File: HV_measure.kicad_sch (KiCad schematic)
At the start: 42 parts

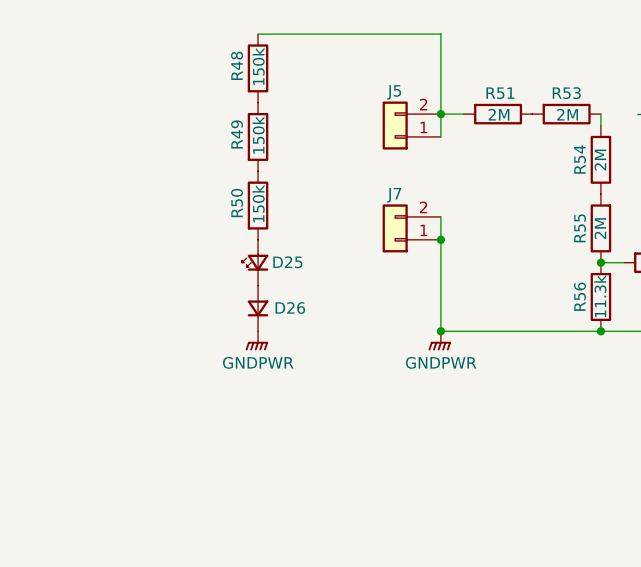
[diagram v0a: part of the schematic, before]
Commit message: VER1.0: добавил аппаратную защиту
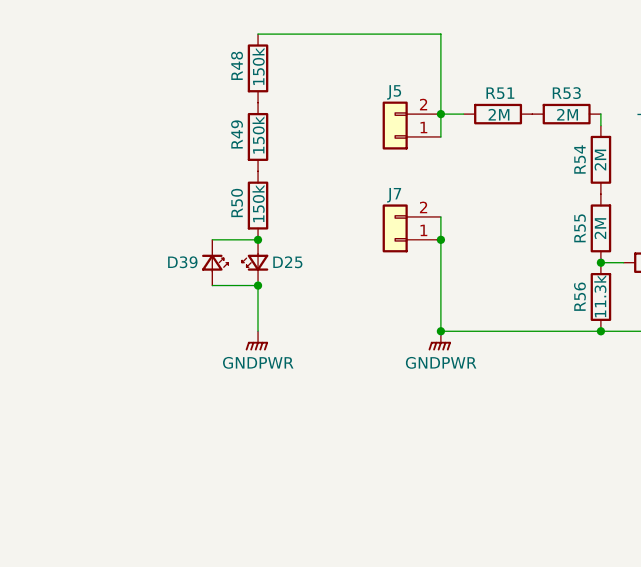
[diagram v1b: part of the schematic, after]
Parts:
- removed D26: (no value), Diode_SMD:D_SMA_Handsoldering, symbol Device:D_Small
- added D39: (no value), LED_SMD:LED_1206_3216Metric_Pad1.42x1.75mm_HandSolder, symbol Device:LED_Small
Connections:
- net GNDPWR: now also D25.1 (K), D39.2 (A)
- net at D25.2 (A), R50.2: now also D39.1 (K)
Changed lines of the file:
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@@
 	)
 	(junction
+		(at 68.58 116.84)
+		(diameter 0)
+		(color 0 0 0 0)
+	)
+	(junction
 		(at 143.51 133.35)
 		(diameter 0)
@@
 	)
 	(junction
+		(at 68.58 111.76)
+		(diameter 0)
+		(color 0 0 0 0)
+	)
+	(junction
 		(at 171.45 99.695)
 		(diameter 0)
@@
 	(wire
 		(pts
+			(xy 63.5 116.84) (xy 68.58 116.84)
+		)
+		(stroke
+			(width 0)
+			(type default)
+		)
+	)
+	(wire
+		(pts
 			(xy 165.1 120.65) (xy 177.8 120.65)
 		)
@@
 	(wire
 		(pts
+			(xy 63.5 111.76) (xy 68.58 111.76)
+		)
+		(stroke
+			(width 0)
+			(type default)
+		)
+	)
+	(wire
+		(pts
 			(xy 152.4 115.57) (xy 152.4 116.84)
 		)
@@
 	(wire
 		(pts
+			(xy 68.58 116.84) (xy 68.58 121.92)
+		)
+		(stroke
+			(width 0)
+			(type default)
+		)
+	)
+	(wire
+		(pts
 			(xy 125.73 46.99) (xy 125.73 48.26)
 		)
@@
 	)
 	(symbol
-		(lib_id "Device:D_Small")
-		(at 68.58 119.38 90)
-		(unit 1)
-		(body_style 1)
-		(exclude_from_sim no)
-		(in_bom yes)
-		(on_board yes)
-		(in_pos_files yes)
-		(dnp no)
-		(property "Reference" "D26"
-			(at 70.358 119.38 90)
-			(show_name no)
-			(do_not_autoplace no)
-			(effects
-				(font
-					(size 1.27 1.27)
-				)
-				(justify right)
-			)
-		)
-		(property "Value" ""
-			(at 71.12 120.65 90)
-			(hide yes)
-			(show_name no)
-			(do_not_autoplace no)
-			(effects
-				(font
-					(size 1.27 1.27)
-				)
-				(justify right)
-			)
-		)
-		(property "Footprint" "Diode_SMD:D_SMA_Handsoldering"
-			(at 68.58 119.38 90)
-			(hide yes)
-			(show_name no)
-			(do_not_autoplace no)
-			(effects
-				(font
-					(size 1.27 1.27)
-				)
-			)
-		)
-		(property "Datasheet" ""
-			(at 68.58 119.38 90)
-			(hide yes)
-			(show_name no)
-			(do_not_autoplace no)
-			(effects
-				(font
-					(size 1.27 1.27)
-				)
-			)
-		)
-		(property "Description" "Diode, small symbol"
-			(at 68.58 119.38 0)
-			(hide yes)
-			(show_name no)
-			(do_not_autoplace no)
-			(effects
-				(font
-					(size 1.27 1.27)
-				)
-			)
-		)
-		(property "Sim.Device" "D"
-			(at 68.58 119.38 0)
-			(hide yes)
-			(show_name no)
-			(do_not_autoplace no)
-			(effects
-				(font
-					(size 1.27 1.27)
-				)
-			)
-		)
-		(property "Sim.Pins" "1=K 2=A"
-			(at 68.58 119.38 0)
-			(hide yes)
-			(show_name no)
-			(do_not_autoplace no)
-			(effects
-				(font
-					(size 1.27 1.27)
-				)
-			)
-		)
-		(property "Description P/N" "Diode"
-			(at 68.58 119.38 90)
-			(hide yes)
-			(show_name no)
-			(do_not_autoplace no)
-			(effects
-				(font
-					(size 1.27 1.27)
-				)
-			)
-		)
-		(property "Product Name" "S1M"
-			(at 68.58 119.38 90)
-			(hide yes)
-			(show_name no)
-			(do_not_autoplace no)
-			(effects
-				(font
-					(size 1.27 1.27)
-				)
-			)
-		)
-		(pin "2"
-		)
-		(pin "1"
-		)
-		(instances
-			(project "PSFB_MCU"
-				(path "/1f44d793-713f-4781-bd7e-20142de81965/70b7ff82-f266-429f-9b56-1fc4058a165c"
-					(reference "D26")
-					(unit 1)
-				)
-			)
-		)
-	)
-	(symbol
 		(lib_id "power:GND")
 		(at 185.42 128.27 0)
@@
 					(unit 1)
 				)
+			)
+		)
+	)
+	(symbol
+		(lib_id "Device:LED_Small")
+		(at 63.5 114.3 270)
+		(unit 1)
+		(body_style 1)
+		(exclude_from_sim no)
+		(in_bom yes)
+		(on_board yes)
+		(in_pos_files yes)
+		(dnp no)
+		(property "Reference" "D39"
+			(at 61.976 114.3 90)
+			(show_name no)
+			(do_not_autoplace no)
+			(effects
+				(font
+					(size 1.27 1.27)
+				)
+				(justify right)
+			)
+		)
+		(property "Value" ""
+			(at 60.96 113.0935 90)
+			(hide yes)
+			(show_name no)
+			(do_not_autoplace no)
+			(effects
+				(font
+					(size 1.27 1.27)
+				)
+				(justify right)
+			)
+		)
+		(property "Footprint" "LED_SMD:LED_1206_3216Metric_Pad1.42x1.75mm_HandSolder"
+			(at 63.5 114.3 90)
+			(hide yes)
+			(show_name no)
+			(do_not_autoplace no)
+			(effects
+				(font
+					(size 1.27 1.27)
+				)
+			)
+		)
+		(property "Datasheet" ""
+			(at 63.5 114.3 90)
+			(hide yes)
+			(show_name no)
+			(do_not_autoplace no)
+			(effects
+				(font
+					(size 1.27 1.27)
+				)
+			)
+		)
+		(property "Description" "Red LED"
+			(at 63.5 114.3 0)
+			(hide yes)
+			(show_name no)
+			(do_not_autoplace no)
+			(effects
+				(font
+					(size 1.27 1.27)
+				)
+			)
+		)
+		(property "Sim.Pin" "1=K 2=A"
+			(at 63.5 114.3 0)
+			(hide yes)
+			(show_name no)
+			(do_not_autoplace no)
+			(effects
+				(font
+					(size 1.27 1.27)
+				)
+			)
+		)
+		(property "Description P/N" "Red LED"
+			(at 63.5 114.3 90)
+			(hide yes)
+			(show_name no)
+			(do_not_autoplace no)
+			(effects
+				(font
+					(size 1.27 1.27)
+				)
+			)
+		)
+		(property "Product Name" "TO-3216BC-MRE"
+			(at 63.5 114.3 90)
+			(hide yes)
+			(show_name no)
+			(do_not_autoplace no)
+			(effects
+				(font
+					(size 1.27 1.27)
+				)
+			)
+		)
+		(pin "2"
+		)
+		(pin "1"
+		)
+		(instances
+			(project "PSFB_MCU"
+				(path "/1f44d793-713f-4781-bd7e-20142de81965/70b7ff82-f266-429f-9b56-1fc4058a165c"
+					(reference "D39")
+					(unit 1)
+				)

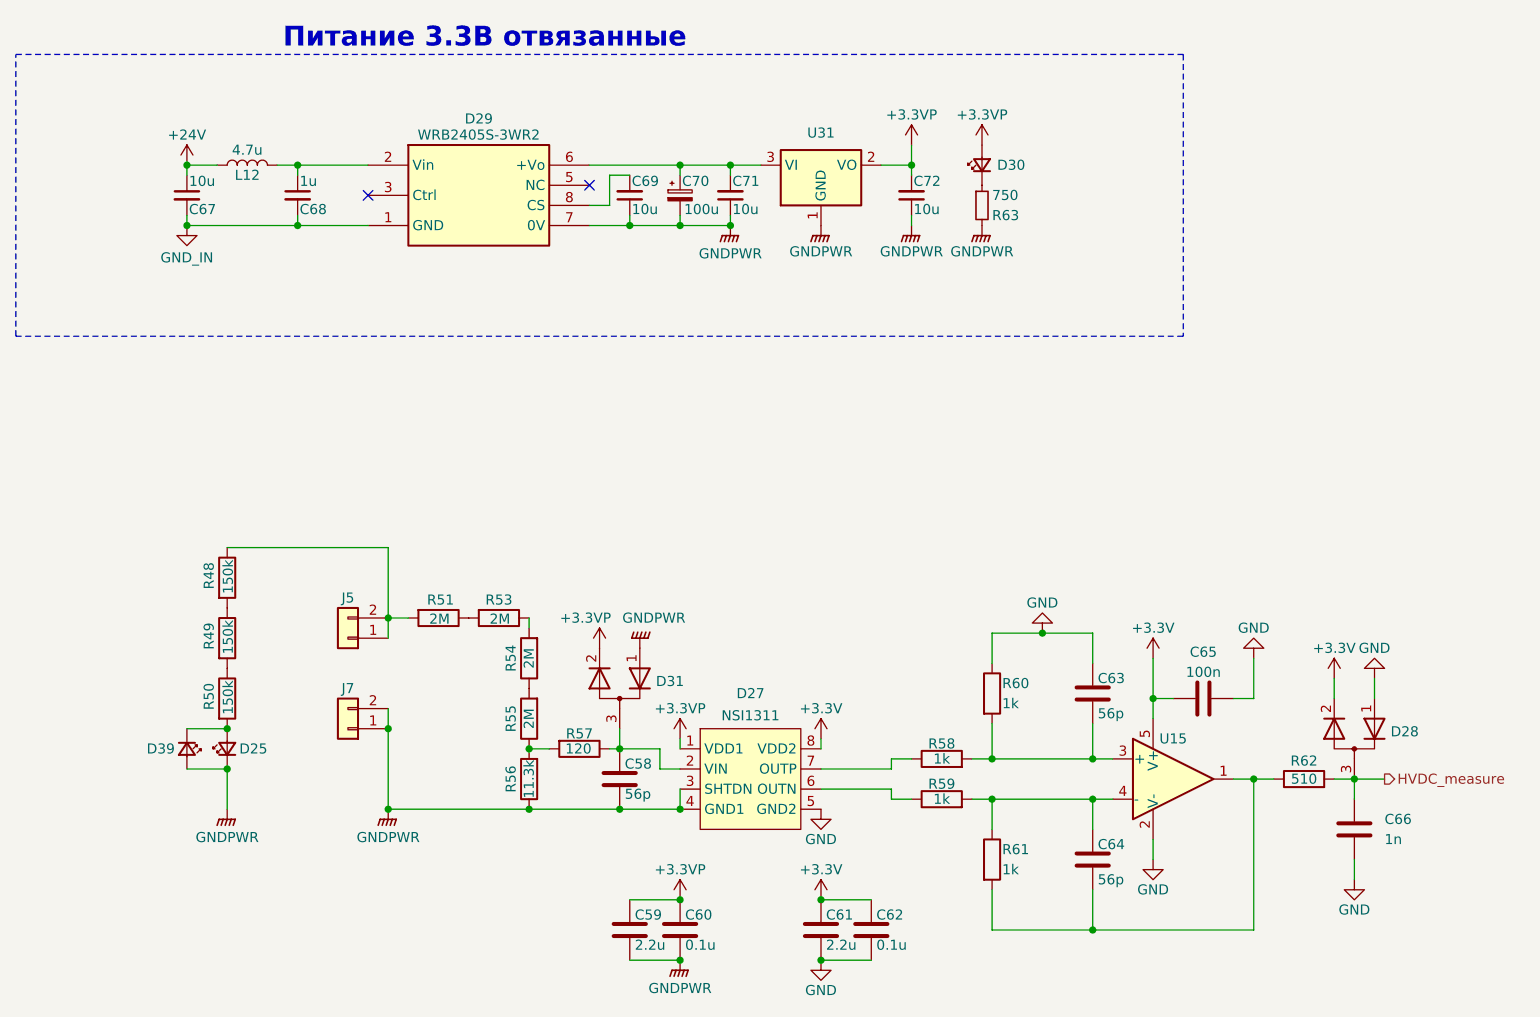
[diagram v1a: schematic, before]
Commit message: VER1.0: добавил разделение питания VDD и VDDA
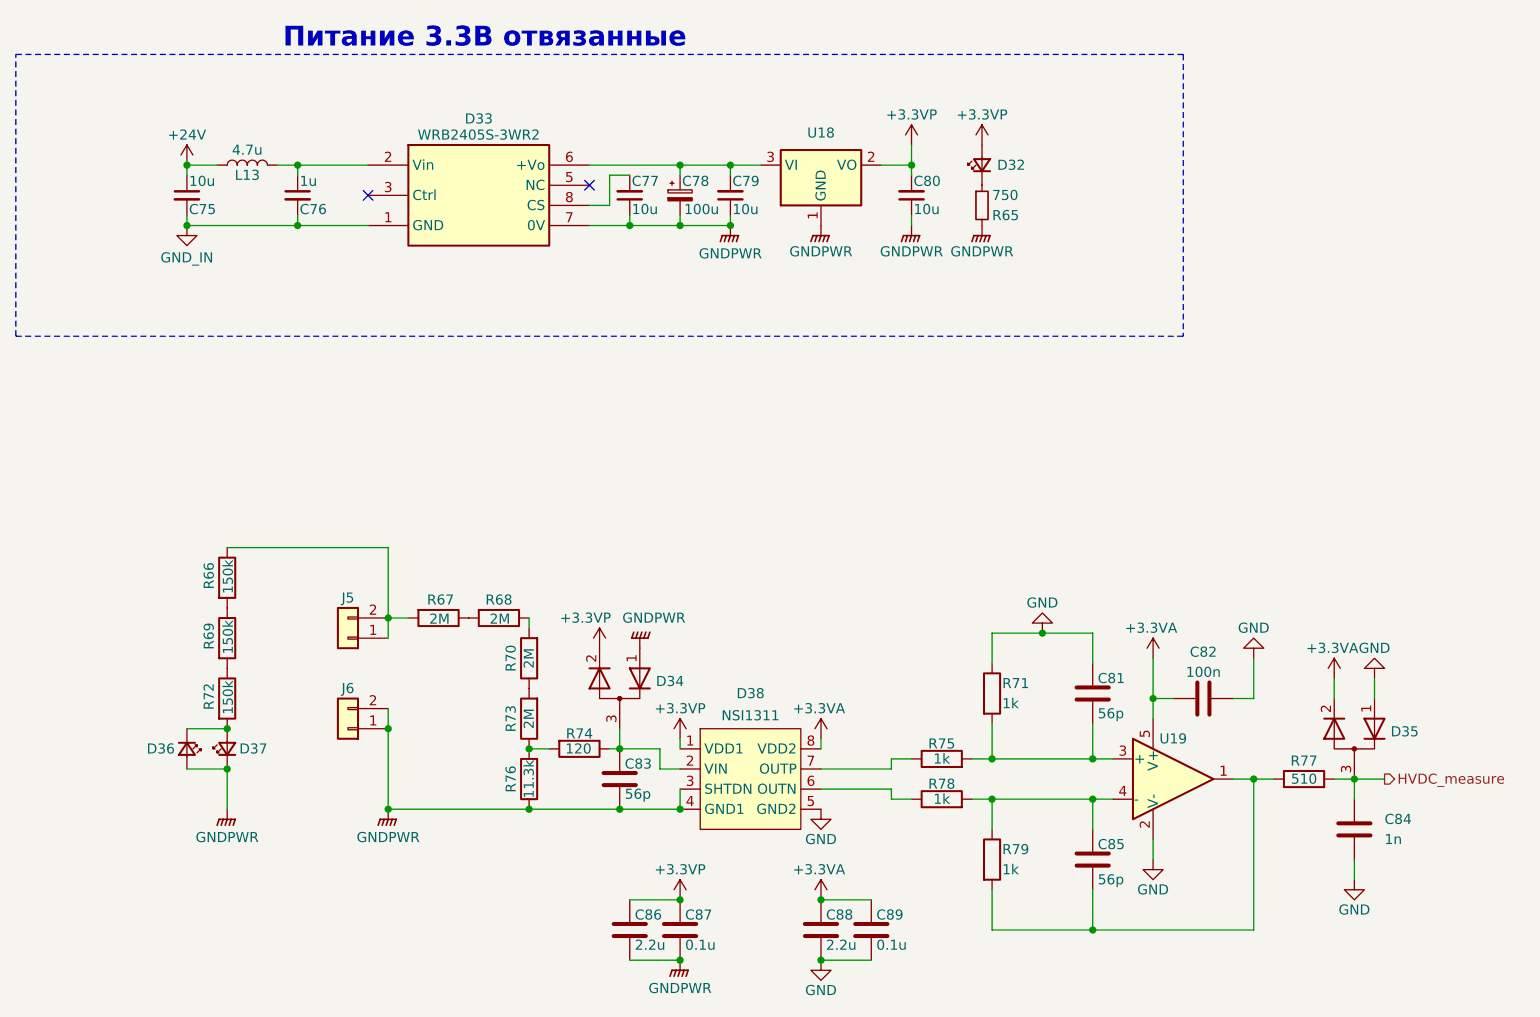
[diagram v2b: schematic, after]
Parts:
- C75: renamed from C67; Description P/N Capacitor SMD 50V -> Capacitor SMD 25V
- C77: renamed from C69; Description P/N Capacitor SMD 50V -> Capacitor SMD 25V
- C78: renamed from C70; Description P/N Polarized capacitor -> Capacitor tantalum SMD 6.3V; Product Name 293D107X96R3B2TE3 -> 6TPE100MWB
- C79: renamed from C71; Description P/N Capacitor SMD 50V -> Capacitor SMD 25V
- C80: renamed from C72; Description P/N Capacitor SMD 50V -> Capacitor SMD 25V
- C81: renamed from C63; Description P/N Capacitor SMD 50V -> Capacitor SMD 25V
- C82: renamed from C65; Description P/N Capacitor SMD 50V -> Capacitor SMD 25V
- C83: renamed from C58; Description P/N Capacitor SMD 50V -> Capacitor SMD 25V
- C84: renamed from C66; Description P/N Capacitor SMD 50V -> Capacitor SMD 25V
- C85: renamed from C64; Description P/N Capacitor SMD 50V -> Capacitor SMD 25V
- C86: renamed from C59; Description P/N Capacitor SMD 50V -> Capacitor SMD 25V
- C87: renamed from C60; Description P/N Capacitor SMD 50V -> Capacitor SMD 25V
- C88: renamed from C61; Description P/N Capacitor SMD 50V -> Capacitor SMD 25V
- C89: renamed from C62; Description P/N Capacitor SMD 50V -> Capacitor SMD 25V
- R65: renamed from R63; Description P/N Resistor SMD -> Resistor SMD 1%
- R66: renamed from R48; Description P/N Resistor SMD -> Resistor SMD 1%
- R67: renamed from R51; Description P/N Resistor SMD -> Resistor SMD 0.1%
- R68: renamed from R53; Description P/N Resistor SMD -> Resistor SMD 0.1%
- R69: renamed from R49; Description P/N Resistor SMD -> Resistor SMD 1%
- R70: renamed from R54; Description P/N Resistor SMD -> Resistor SMD 0.1%
- R71: renamed from R60; Description P/N Resistor SMD -> Resistor SMD 1%
- R72: renamed from R50; Description P/N Resistor SMD -> Resistor SMD 1%
- R73: renamed from R55; Description P/N Resistor SMD -> Resistor SMD 0.1%
- R74: renamed from R57; Description P/N Resistor SMD -> Resistor SMD 1%
- R75: renamed from R58; Description P/N Resistor SMD -> Resistor SMD 1%
- R76: renamed from R56; Description P/N Resistor SMD -> Resistor SMD 0.1%
- R77: renamed from R62; Description P/N Resistor SMD -> Resistor SMD 1%
- R78: renamed from R59; Description P/N Resistor SMD -> Resistor SMD 1%
- R79: renamed from R61; Description P/N Resistor SMD -> Resistor SMD 1%
- U19: renamed from U15; Product Name OPA333xxDBV -> OPA333AIDBVR
- renumbered C68 to C76, D30 to D32, D29 to D33, D31 to D34, D28 to D35, D39 to D36, D25 to D37, D27 to D38, J7 to J6, L12 to L13, U31 to U18
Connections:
- net +3.3V renamed +3.3VA

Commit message: VER1.0: раскидал компоненты на плате
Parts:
- C78: footprint Capacitor_Tantalum_SMD:CP_EIA-3528-21_Kemet-B_Pad1.50x2.35mm_HandSolder -> Capacitor_Tantalum_SMD:CP_EIA-3528-21_Kemet-B_HandSolder
- J5, J6: footprint Connector_My:Mini-Fit_01x02_Vertical -> Connector_Molex:Molex_Mini-Fit_Jr_5569-02A2_2x01_P4.20mm_Horizontal
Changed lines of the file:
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@@
 			)
 		)
-		(property "Footprint" "Connector_My:Mini-Fit_01x02_Vertical"
+		(property "Footprint" "Connector_Molex:Molex_Mini-Fit_Jr_5569-02A2_2x01_P4.20mm_Horizontal"
 			(at 83.82 111.76 0)
 			(hide yes)
@@
 			)
 		)
+		(property "Function" ""
+			(at 83.82 111.76 0)
+			(hide yes)
+			(show_name no)
+			(do_not_autoplace no)
+			(effects
+				(font
+					(size 1.27 1.27)
+				)
+			)
+		)
 		(pin "2"
 		)
@@
 			)
 		)
-		(property "Footprint" "Capacitor_Tantalum_SMD:CP_EIA-3528-21_Kemet-B_Pad1.50x2.35mm_HandSolder"
+		(property "Footprint" "Capacitor_Tantalum_SMD:CP_EIA-3528-21_Kemet-B_HandSolder"
 			(at 125.73 44.45 0)
 			(hide yes)
@@
 			)
 		)
-		(property "Footprint" "Connector_My:Mini-Fit_01x02_Vertical"
+		(property "Footprint" "Connector_Molex:Molex_Mini-Fit_Jr_5569-02A2_2x01_P4.20mm_Horizontal"
 			(at 83.82 100.33 0)
 			(hide yes)
@@
 			(at 83.82 100.33 0)
 			(hide yes)
+			(show_name no)
+			(do_not_autoplace no)
+			(effects
+				(font
+					(size 1.27 1.27)
+				)
+			)
+		)
+		(property "Function" ""
+			(at 83.82 100.33 0)
+			(hide yes)

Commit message: VER1.0: отредактировал BOM
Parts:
- J5, J6: Product Name DS1073-01-2x1-MVT6 -> DS1073-01-2x1MR2T6
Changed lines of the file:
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@@
 			)
 		)
-		(property "Product Name" "DS1073-01-2x1-MVT6"
+		(property "Product Name" "DS1073-01-2x1MR2T6"
 			(at 83.82 111.76 0)
 			(hide yes)
@@
 			)
 		)
-		(property "Product Name" "DS1073-01-2x1-MVT6"
+		(property "Product Name" "DS1073-01-2x1MR2T6"
 			(at 83.82 100.33 0)
 			(hide yes)
